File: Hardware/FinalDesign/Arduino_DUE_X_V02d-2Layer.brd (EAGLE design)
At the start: 83.5 x 55.2 mm, 98 parts, among them IC1 LMV358IDGKR, IC10 74LVC1G125DCK, IC4 NCP1117ST33T3G -3V3, IC6 ATMEGA16U2-MU, J3 USB-MICRO B, T3 FDN340P, U1 ATSAM3X8EA-AU, U2 MCP2551, U3 LCD_DISPLAY, U4 MCP2551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

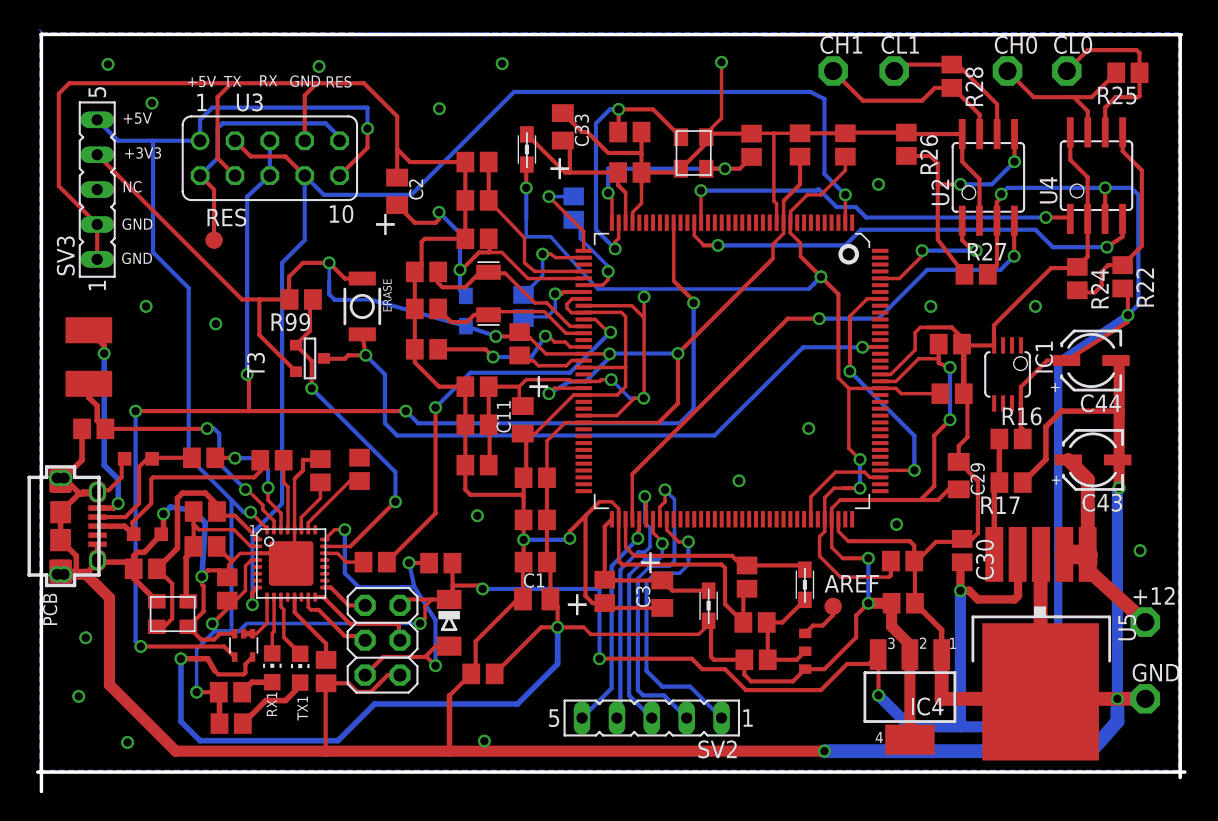
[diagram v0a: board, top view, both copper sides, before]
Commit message: Made final revisions to board
added +5V and GND terminals for wire harness,
fixed minor issues
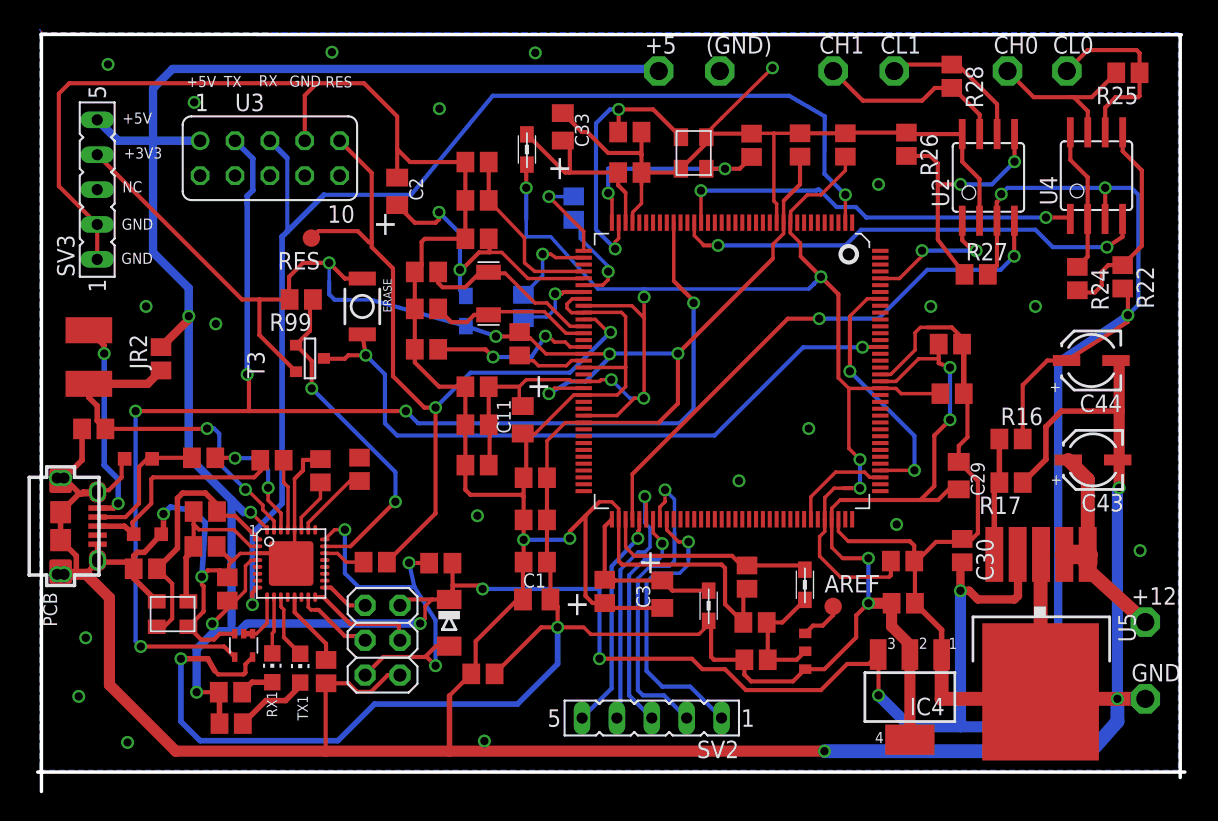
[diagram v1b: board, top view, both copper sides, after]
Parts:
- removed IC1: LMV358IDGKR, linear:MSOP08
- added (GND), +5: TPPAD1-13, testpad:P1-13
- added JR2: 0R, SmartPrj:R0805
- C30: value 100n -> 47u
- moved RES 7.09 mm to (19.7, 39.3), turned to 180 degrees
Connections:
- removed net RES: RES.TP, U3.2, U3.9
- net +3V3: now also T3.1; no longer T3.2
- net +5V: now also +5.TP, JR2.2; no longer IC1.8, U3.10
- net ERASE_CMD: now also T3.2; no longer T3.3
- net ERASE_S: now also T3.3; no longer T3.1
- net GND: now also (GND).TP; no longer IC1.4, U3.4
- net MASTER-RESET: now also RES.TP, U3.9
- net RX: now also U3.3; no longer U3.5, U3.6
- net TX: now also U3.5; no longer U3.3, U3.8
- net USBVCCU2: now also JR2.1
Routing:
- net MASTER-RESET: track 30.1 -> 57.8 mm
- net +5V: track 261.1 -> 286.2 mm
- net RES: track 18.8 -> 0.00 mm
- net GND: track 550.5 -> 532.4 mm
- net USBVCCU2: track 21.0 -> 26.6 mm
- net TX: track 91.6 -> 89.4 mm
